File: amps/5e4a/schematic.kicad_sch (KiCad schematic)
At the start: 64 parts, among them T1 PT, T3 OT

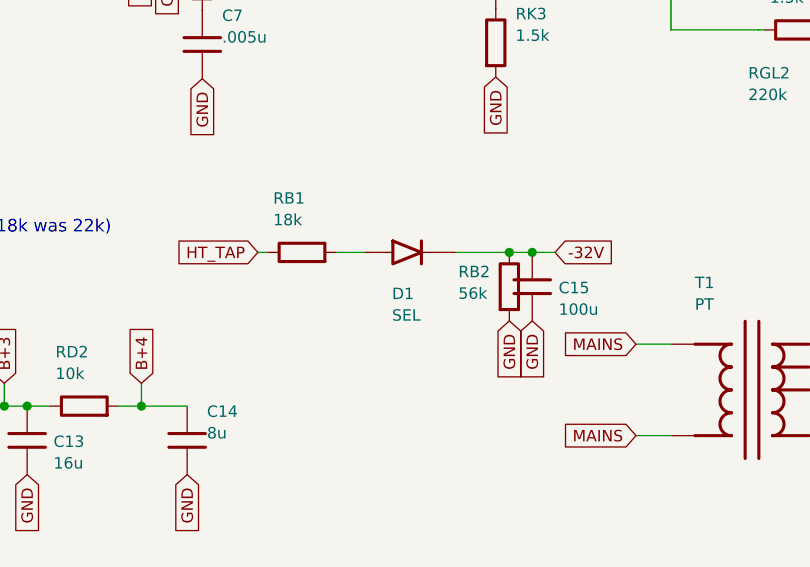
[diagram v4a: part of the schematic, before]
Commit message: Fix: 17 bias rectifiers and six HT diodes drawn backwards; the 6G6-B and 6G4 bias rows as their drawings show; AA1164 V4 units
Rectifier polarity has no gate. The netlists model every supply as an ideal
source, the sheet-vs-board check treats a two-terminal part as unordered, and
the boards' `cathode:` fields were copied from the sheets. Measured over all
68 diodes on 40 sheets: 18 negative-bias rectifiers had the cathode on the
negative node (a diode that way round would charge the node POSITIVE), and all
six 6G6-B HT diodes pointed away from B+. The printed negative bias on each of
those sheets falsifies the drawn orientation; the nine bias rectifiers already
right (AA1164, AA864, AB165, B15N, DR103, JTM100, M1959, M2204, 6G6-B) show
the idiom. Flipped: 5E4-A, 5E5-A, 5E6-A, 5F10, 5F4, 5F6, 5F6-A, 5F8-A, 5G9,
6G2, 6G3, 6G4, 6G5, AA964, AB763, AB763 Super, AB763 Twin, JTM45 (the
M1987's is with the Marshall board repair) and the 6G6-B's DR1-DR6. The
5F8-A board, which had copied its sheet, has the band moved to the tap side;
the other boards' bands are with the board-repair wave. A gate is next.

6G6-B bias. E-FB (6431x3364): the 1K 1W rises from TR1's SECOND secondary
terminal, a bias tap between the upper HT end and the grounded centre tap,
to the diode's + end. The sheet fed the diode from the HT end with the 1K
after it. T1 now carries its tap pin and the row reads tap -> 1K -> diode ->
-54 V. (The triage had read "HT end"; the native crop shows the tap.)

6G4 bias. A-FJ, read natively: tap -> rectifier -> 8 uF -> 10K -> the -55 V
node, which carries a second 8 uF and the 56K to ground as a bleeder. The
sheet fed the rectifier from an HT end, drew the 56K in series and carried
one capacitor. CBIAS2 joins the parts list, and RBIAS1's role now says
bleeder.

AA1164 V4. The K-FD sheet prints the phase inverter 7/6/8 and the tremolo
oscillator 2/1/3 (5554x4346); the sheet had them the other way round.

Gates: check_schematics 40/0 (+selftest), verify_schematic_nets 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
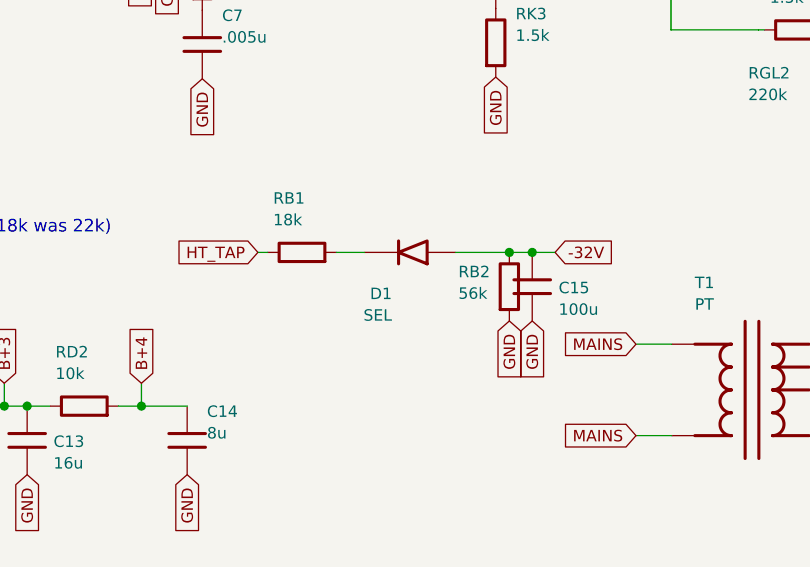
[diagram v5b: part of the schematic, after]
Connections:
- net -32V: now also D1.1 (A); no longer D1.2 (K)
- net at RB1.2: now also D1.2 (K); no longer D1.1 (A)
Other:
- moved on the sheet: D1
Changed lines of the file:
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@@
   (wire (pts (xy 149.828 106.998) (xy 152.938 106.998))
     (stroke (width 0) (type default)))
-  (symbol (lib_id "cx:DIODE_SS") (at 158.018 106.998 0) (unit 1)
+  (symbol (lib_id "cx:DIODE_SS") (at 158.018 106.998 180) (unit 1)
     (in_bom yes) (on_board yes)
     (property "Reference" "D1" (at 156.018 111.598 0) (effects (font (size 1.27 1.27)) (justify left)))

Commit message: Fix: the 6G5's rectifier was connected to nothing; 17 sheets shorted the mains by naming both leads alike
6G5 power supply. The sheet drew four diodes as a "silicon bridge" whose
HT_A/HT_B labels stopped 6 mm short of their wires. D1/D2's anodes sat on
the tremolo's cathode node (a tremolo wire's end touched the old diode
stub), D3/D4 ran from ground to the reservoir, and TR1's centre tap floated
under an open-pin waiver whose stated reason was the bridge itself.
A-FJ (Schematic Heaven 2153x1437, read enlarged): each HT end of TR1 runs
through a leg of three silicon diodes, every + (cathode) toward the +460 V
reservoir; the centre tap is grounded; TR1's second secondary terminal is a
bias tap feeding the 6G4's network part for part: rectifier, 8-150, 10K,
then 8-150 and a 56K bleeder at the -55 V line. Redrawn as the drawing
shows: D1-D6, TR1 with its tap pin, the centre tap to ground, the bias
network (CBIAS 25 uF -> 8 uF; RBIAS2, CBIAS2, RBIAS1 added), the waiver
deleted, and the notes, meta, netlist header and parts list no longer say
bridge. Not yet carried: the drawing's second 20-600 at the reservoir and
the standby switch (this sheet omits chassis switches by its own note);
and the tremolo ladder still runs through the transformer's corner of the
sheet, a layout clash rather than a connection, queued for its own redraw.

Mains. Two global labels with one name are one net. 16 of 24 power
transformers on the sheets carried a label named MAINS on both primary
leads, so the winding's two pins were one net: 5E4-A, 5E5-A, 5F4, 5G9,
6161, 6G2, 6G3, 6G4, AA1164, AA764, AA764-Vibro, AA964, AB763, AB763
Super, AB763 Twin, GA-40. The 6G5's loop ran from one MAINS label through
switch, fuse and winding back to the same name. No gate models the primary,
so a copy-pasted idiom did this. The second lead is now MAINS N, the AC15's
idiom; the AA1164's and AA964's second AC row, drawn under the first row's
name, is the neutral. The death and across-the-line caps stay on the le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
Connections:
- net MAINS: no longer T1.2 (PRI_2)
- new net MAINS N: T1.2 (PRI_2)
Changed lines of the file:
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@@
   (wire (pts (xy 187.128 127.358) (xy 183.128 127.358))
     (stroke (width 0) (type default)))
-  (global_label "MAINS" (shape input) (at 183.128 127.358 180)
+  (global_label "MAINS N" (shape input) (at 183.128 127.358 180)
     (effects (font (size 1.27 1.27)) (justify right)))
   (wire (pts (xy 204.908 117.198) (xy 216.908 117.198))

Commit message: Fix: give the 5E4-A presence pot and its 0.1 µF designators, draw them on the sheet, and wire the board as the layout sheet does
The 5 kΩ presence pot and its 0.1 µF were "—" annotation rows in bom.yaml and only note text on the sheet. The board placed a VRP stub with no ref, so the sheet-board gate reported it board_only. Both now have refs: VRP (5 kΩ linear) and CP (0.1 µF · 200 V). Both are BOM additions; no value changes.

What the G-EE drawing shows. On the schematic page, crop (3500,500)-(4300,1700), one end of the 5K takes the driver's cathode/feedback node, its wiper carries the .1-200 to ground, and the other end is free. On the layout page, crop (1700,500)-(2500,1700), the pot's left lug is strapped to the wiper and carries the .1 MFD to chassis, and the right lug runs down to the board's cathode eyelet. The board grounded the far lug directly, which put a bare 5 kΩ from V3A's cathode to ground with no capacitor in it. Now the far lug is strapped to the wiper and goes through CP, an off-board part at the pot, to chassis at the bias can's grounded eyelet. The sheet draws VRP from V3A's cathode with the same strap and CP to ground, and its note now names only the 56k NFB as annotation. The caption and notes.md say so.

5E4-A sheet-board: board_only [VRP] -> [], PASS (claimed). verify_schematic_nets PASS. The netlist is unchanged: the presence network was never in it (the layout header already lists it in the excluded annotation layer). Both board drawings, the sheet, site copies and og card are regenerated. FW-19 P10c.

Co-Authored-By: Claude Opus 5.5 <noreply@anthropic.com>
Claude-Session: https://claude.ai/code/session_01KBMfdh37HmCL2iWcBiL5J1
Signed-off-by: AnalogMaker <theanalogmaker@gmail.com>
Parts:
- removed C10: .1u, symbol cx:C
- removed R6s, RKA: 1.5k, symbol cx:R
- removed RD2: 10k, symbol cx:R
- removed RGB: 1M, symbol cx:R
- added CP: .1u, symbol cx:C
- added RB1: 18k, symbol cx:R
- added RGL2: 220k, symbol cx:R
- added RKB: 56k, symbol cx:R
- added T3: OT, symbol cx:OT_PP
- added V4: 6V6GT, symbol cx:PENTODE
- added VRP: 5k presence, symbol cx:POT
- C10: renamed from RGL2; value 220k -> .1u; symbol cx:R -> cx:C
- R6s: renamed from T3; value OT -> 1.5k; symbol cx:OT_PP -> cx:R
- RD2: renamed from RB1; value 18k -> 10k
- RGB: renamed from RKB; value 56k -> 1M
- RKA: renamed from V4; value 6V6GT -> 1.5k; symbol cx:PENTODE -> cx:R
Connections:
- net -32V: now also RGL2.2; no longer C10.2
- net B+1: now also T3.2 (CT); no longer R6s.2 (CT)
- net B+2: now also V4.3 (G2); no longer RKA.3 (G2)
- net B+3: now also RD2.1
- net B+4: now also RD2.2
- net GND: now also CP.2, RKB.2, T3.5 (SEC_C), V4.4 (K); no longer R6s.5 (SEC_C), RGB.2, RKA.4 (K)
- net HT_TAP: now also RB1.1; no longer RD2.1
- net SPKR: now also T3.4 (SEC_H); no longer R6s.4 (SEC_H)
- net at RGB.1: now also C8.1, V3B.2 (G)
- net at V3B.3 (K): now also C10.1, RKA.1
- net at R5s.2, RGL1.1: now also V4.2 (G1); no longer RKA.2 (G1)
- net at RK3.1, V3A.3 (K): now also VRP.3
- net at R6s.1: now also C10.2; no longer RKA.1 (P)
- net at V5.1 (P): now also T3.3 (PRI_B); no longer R6s.3 (PRI_B)
- net at V5.2 (G1): now also R6s.2, RGL2.1; no longer C10.1
- net at D1.2 (K): now also RB1.2; no longer RD2.2
- new net: RGB.2, RKA.2, RKB.1
- new net: CP.1, VRP.1, VRP.2 (W)
- new net: T3.1 (PRI_A), V4.1 (P)
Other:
- note added: "56k NFB from the speaker lands on V3A's cathode (annotation)"
- note removed: "56k NFB from the speaker + 5k presence (0.1 µF on its wiper) land on V3A's cathode (annotation)"
- moved on the sheet: RD2, RGB
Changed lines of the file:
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@@
   (global_label "GND" (shape input) (at 167.548 87.518 270)
+    (effects (font (size 1.27 1.27)) (justify right)))
+  (junction (at 167.548 79.898) (diameter 1.013) (color 0 0 0 0))
+  (wire (pts (xy 167.548 79.898) (xy 159.018 79.898))
+    (stroke (width 0) (type default)))
+  (symbol (lib_id "cx:POT") (at 159.018 83.708 180) (unit 1)
+    (in_bom yes) (on_board yes)
+    (property "Reference" "VRP" (at 143.349 82.068 180) (effects (font (size 1.27 1.27)) (justify left)))
+    (property "Value" "5k presence" (at 143.349 84.468 180) (effects (font (size 1.27 1.27)) (justify left))))
+  (wire (pts (xy 153.938 83.708) (xy 152.018 83.708))
+    (stroke (width 0) (type default)))
+  (wire (pts (xy 152.018 83.708) (xy 152.018 87.518))
+    (stroke (width 0) (type default)))
+  (wire (pts (xy 152.018 87.518) (xy 159.018 87.518))
+    (stroke (width 0) (type default)))
+  (junction (at 159.018 87.518) (diameter 1.013) (color 0 0 0 0))
+  (symbol (lib_id "cx:C") (at 159.018 91.328 0) (unit 1)
+    (in_bom yes) (on_board yes)
+    (property "Reference" "CP" (at 161.218 88.128 0) (effects (font (size 1.27 1.27)) (justify left)))
+    (property "Value" ".1u" (at 161.218 90.528 0) (effects (font (size 1.27 1.27)) (justify left))))
+  (global_label "GND" (shape input) (at 159.018 95.138 270)
     (effects (font (size 1.27 1.27)) (justify right)))
   (junction (at 167.548 61.178) (diameter 1.013) (color 0 0 0 0))
@@
   (text "4" (at 46.478 107.708 0)
     (effects (font (size 1.1 1.1)) (justify left)))
-  (text "56k NFB from the speaker + 5k presence (0.1 µF on its wiper) land on V3A's cathode (annotation)" (at 12.7 142.856 0)
+  (text "56k NFB from the speaker lands on V3A's cathode (annotation)" (at 12.7 142.856 0)
     (effects (font (size 1.2 1.2)) (justify left)))
   (text "Heaters, mains switch, fuse and standby omitted — see the netlist and the sources list" (at 12.7 147.256 0)

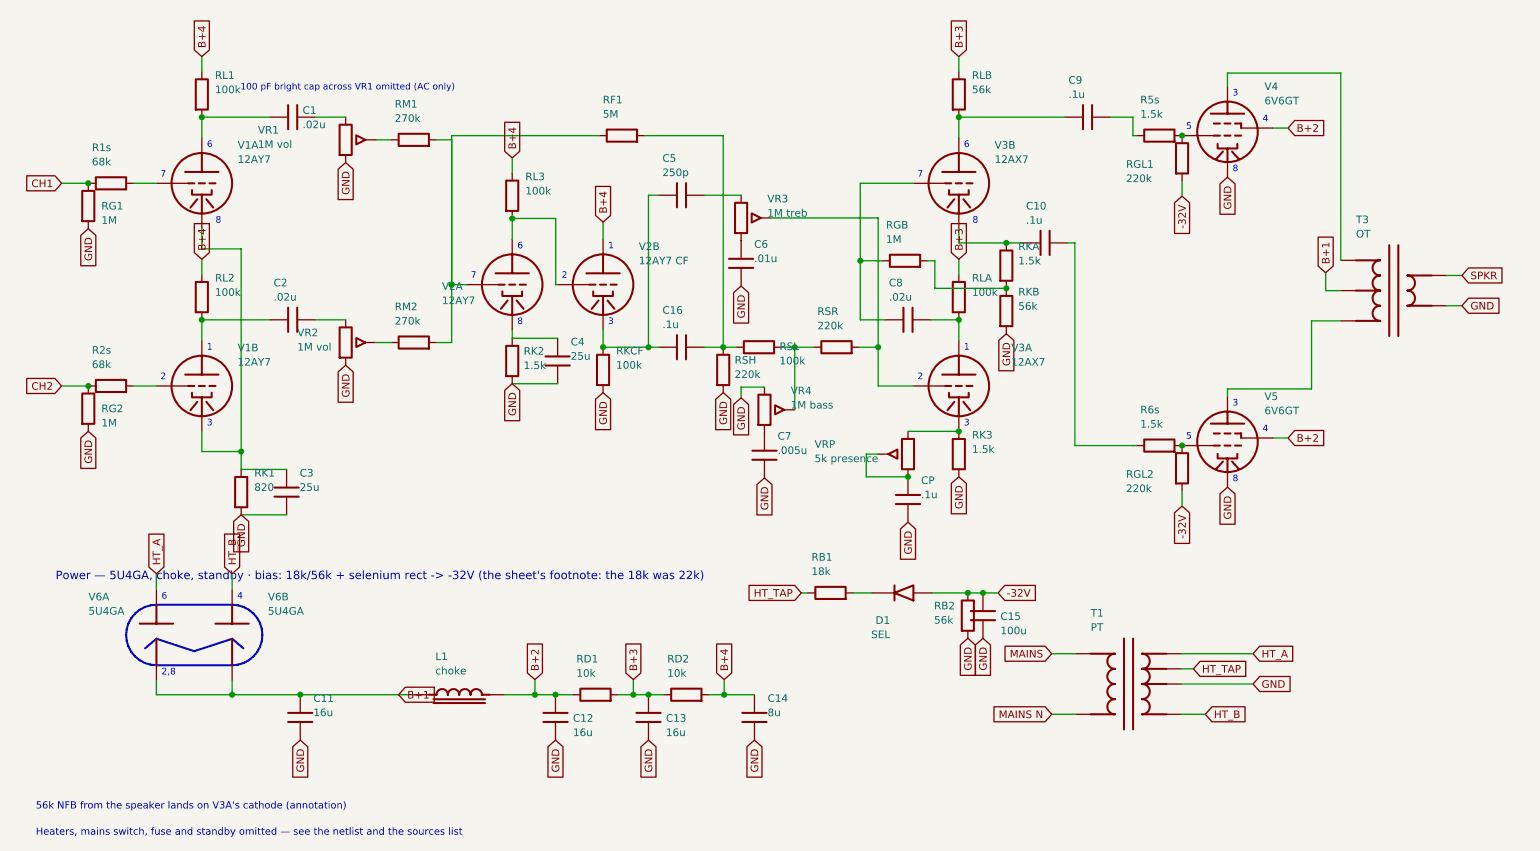
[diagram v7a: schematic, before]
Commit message: 5E4-A: jack-2 stoppers; OT centre tap on the choke's output (V1 audit)
G-EE draws four input jacks and four 68 Ks, two per channel, on both pages
(schematic 6232x3528 crop 0,820,1900,2600; layout 6210x3501 crop
4800,480,6200,2500). The corpus carried one 68 K per channel, and the BOM
note and the notes said the schematic draws one jack per channel. R3s and
R4s (68 k) are added to the BOM, the sheet and the board (declared
series_bridge); the board widens by two columns.

Both pages put the output-transformer centre tap on the +385 V node with
the screens: the schematic runs it into the screen line (crop
4900,750,5450,1650) and the layout letters the OT's RED lead onto the right
6V6GT's pin 4 (crop 1150,2400,2300,3150). The sheet, the board and the
netlist hung it on +390, the reservoir side of the choke. All three now
take B+2; the plates follow (primary DCR omitted). BP2 lands at 385.0 V
against the printed 385; the worst node is KAY at 8.7 %, so
max_deviation_pct 10.0 -> 8.7 as the gate requires. Status, date and
claims untouched.

Text: no page prints a pot taper, so VR1/VR2/VR4/VRP say so like VR3;
stale 6L6G and 4.7M comments corrected.

Co-Authored-By: Claude Opus 5.5 <noreply@anthropic.com>
Claude-Session: https://claude.ai/code/session_01KBMfdh37HmCL2iWcBiL5J1
Signed-off-by: AnalogMaker <theanalogmaker@gmail.com>
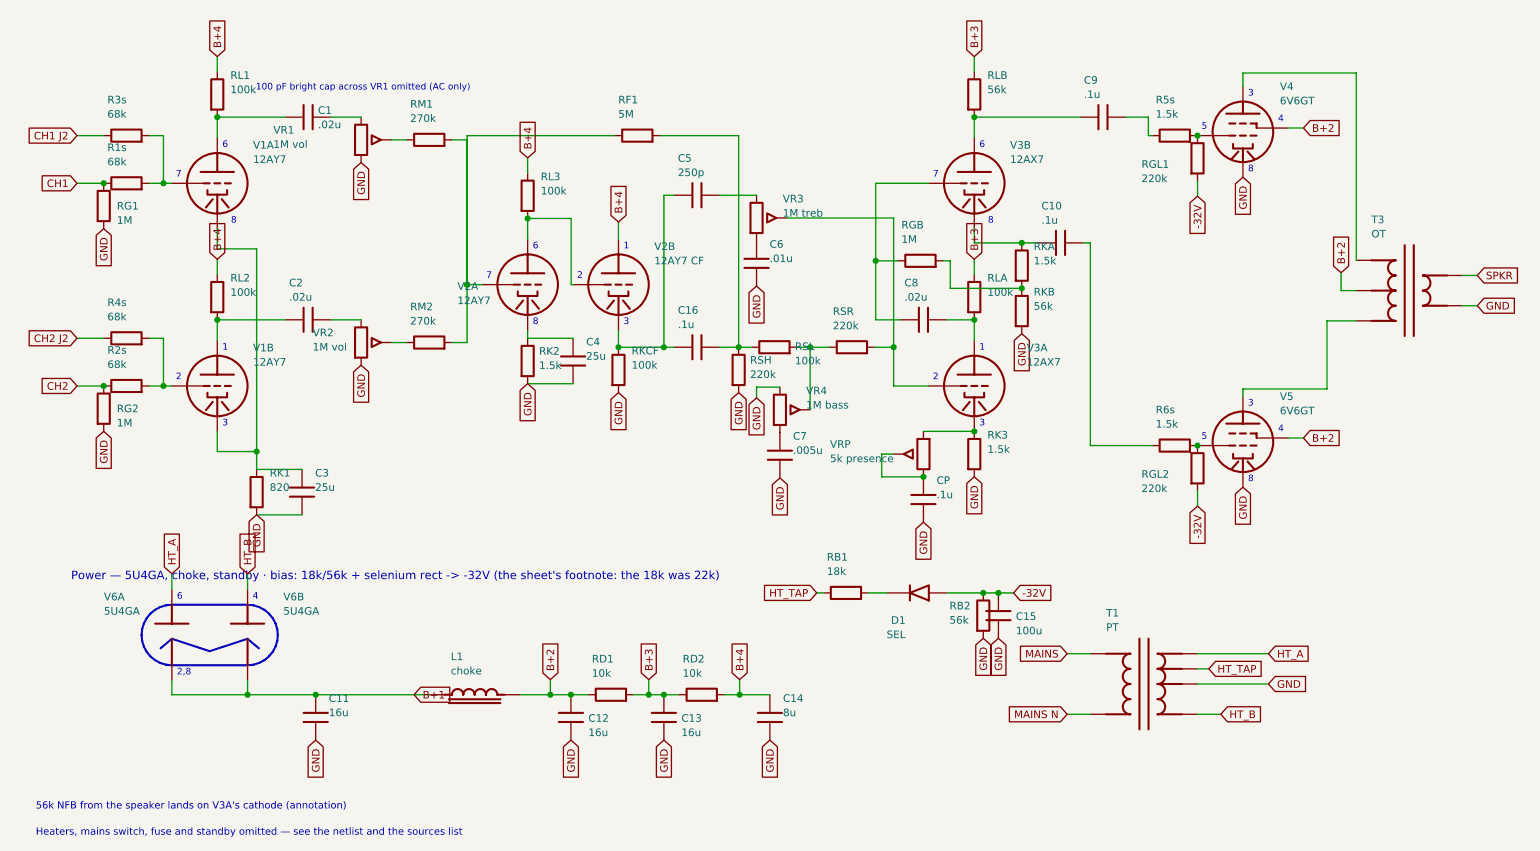
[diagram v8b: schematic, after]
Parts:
- removed C11, C13: 16u, symbol cx:C
- removed C14: 8u, symbol cx:C
- removed C5: 250p, symbol cx:C
- removed C7: .005u, symbol cx:C
- removed C8: .02u, symbol cx:C
- removed C9: .1u, symbol cx:C
- removed RB1: 18k, symbol cx:R
- removed RK1: 820, symbol cx:R
- removed RKCF, RL1: 100k, symbol cx:R
- removed RM2: 270k, symbol cx:R
- removed VR4: 1M bass, symbol cx:POT
- added C10, C16: .1u, symbol cx:C
- added C15: 100u, symbol cx:C
- added C3: 25u, symbol cx:C
- added D1: SEL, symbol cx:DIODE_SS
- added R3s, R4s: 68k, symbol cx:R
- added RD1: 10k, symbol cx:R
- added RKA: 1.5k, symbol cx:R
- added RL3, RLA, RSL: 100k, symbol cx:R
- added RLB: 56k, symbol cx:R
- added T1: PT, symbol cx:PT
- added VR1: 1M vol, symbol cx:POT
- C11: renamed from RD1; value 10k -> 16u; symbol cx:R -> cx:C
- C13: renamed from D1; value SEL -> 16u; symbol cx:DIODE_SS -> cx:C
- C14: renamed from C15; value 100u -> 8u
- C5: renamed from RSL; value 100k -> 250p; symbol cx:R -> cx:C
- C7: renamed from RLB; value 56k -> .005u; symbol cx:R -> cx:C
- C8: renamed from RKA; value 1.5k -> .02u; symbol cx:R -> cx:C
- RB1: renamed from T1; value PT -> 18k; symbol cx:PT -> cx:R
- RK1: renamed from RL3; value 100k -> 820
- RKCF: renamed from C16; value .1u -> 100k; symbol cx:C -> cx:R
- RL1: renamed from VR1; value 1M vol -> 100k; symbol cx:POT -> cx:R
- RM2: renamed from C3; value 25u -> 270k; symbol cx:C -> cx:R
- VR4: renamed from RLA; value 100k -> 1M bass; symbol cx:R -> cx:POT
- renumbered C10 to C9
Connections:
- net -32V: now also C15.1, D1.1 (A); no longer C13.1 (A), C14.1
- net B+1: now also C11.1; no longer T3.2 (CT)
- net B+2: now also T3.2 (CT), RD1.1; no longer C11.1
- net B+3: now also C13.1, RD1.2, RLA.1, RLB.1; no longer C11.2, C7.1, VR4.1
- net B+4: now also C14.1, RL1.1, RL3.1; no longer RK1.1
- net GND: now also C11.2, C13.2, C7.2, RK1.2, RKCF.2, VR4.1, C15.2, C3.2, T1.4 (HT_CT), VR1.3; no longer RB1.4 (HT_CT), RL1.3, RM2.2
- net HT_A: now also T1.3 (HT_A); no longer RB1.3 (HT_A)
- net HT_B: now also T1.5 (HT_B); no longer RB1.5 (HT_B)
- net HT_TAP: now also RB1.1, T1.6 (HT_TAP); no longer RB1.6 (HT_TAP)
- net MAINS: now also T1.1 (PRI_1); no longer RB1.1 (PRI_1)
- net MAINS N: now also T1.2 (PRI_2); no longer RB1.2 (PRI_2)
- net at RGB.1, V3B.2 (G): now also C8.1
- net at RGB.2, RKB.1: now also RKA.2; no longer C8.2
- net at C1.1, V1A.1 (P): now also RL1.2
- net at C1.2: now also VR1.1; no longer RL1.1
- net at RM1.1: now also VR1.2 (W); no longer RL1.2 (W)
- net at R1s.2, V1A.2 (G): now also R3s.2
- net at V1A.3 (K), V1B.3 (K): now also RK1.1, C3.1; no longer RM2.1
- net at VR2.2 (W): now also RM2.1
- net at RF1.1, RM1.2, V2A.2 (G): now also RM2.2
- net at R5s.1: now also C9.2
- net at V3B.1 (P): now also C9.1, RLB.2; no longer C7.2
- net at V2A.1 (P), V2B.2 (G): now also RL3.2; no longer RK1.2
- net at RKCF.1, V2B.3 (K): now also C5.1, C16.1
- net at V3A.1 (P): now also C8.2, RLA.2; no longer VR4.2
- net at RSR.1: now also VR4.2 (W), RSL.2; no longer C5.2
- net at R2s.2, V1B.2 (G): now also R4s.2
- net at VR3.1: now also C5.2
- net at RF1.2, RSH.1: now also C16.2, RSL.1; no longer C5.1, RKCF.2
- net at R6s.1: now also C10.2; no longer C9.2
- new net: C10.1, RKA.1, V3B.3 (K)
- new net: C7.1, VR4.3
- new net: D1.2 (K), RB1.2
- new net CH1 J2: R3s.1
- new net CH2 J2: R4s.1
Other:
- moved on the sheet: C13, C14, C9, R1s, RK1, V1A
